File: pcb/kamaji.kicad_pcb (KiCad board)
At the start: 2 copper layers, 130 x 110 mm, 31 parts, among them J1 RJ10, J2 RJ10, J3 RJ10, J4 RJ10, J5 RJ10, Q1 TIP120, Q2 TIP120, SW1 CTRL1, SW2 CTRL2, SW3 CTRL3, U1 ATMEGA328P-PU

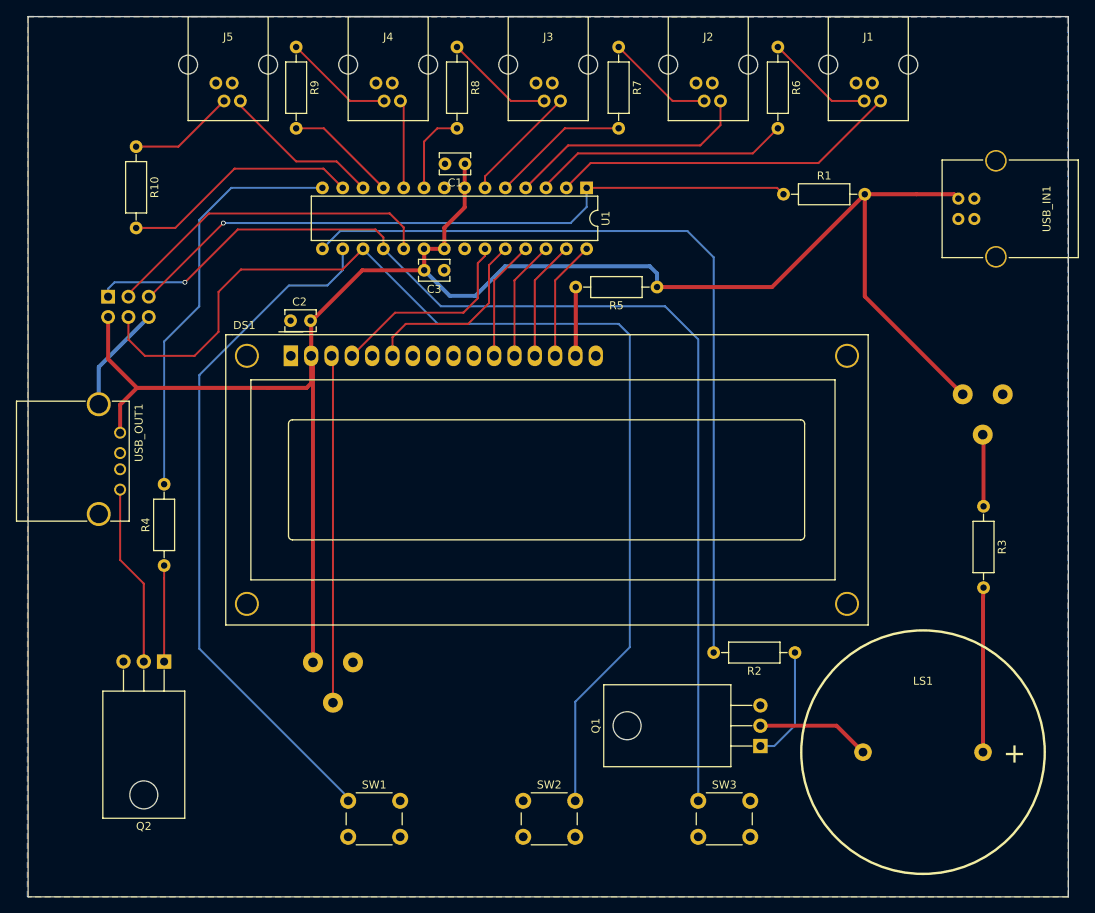
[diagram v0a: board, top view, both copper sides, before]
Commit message: add mounting holes
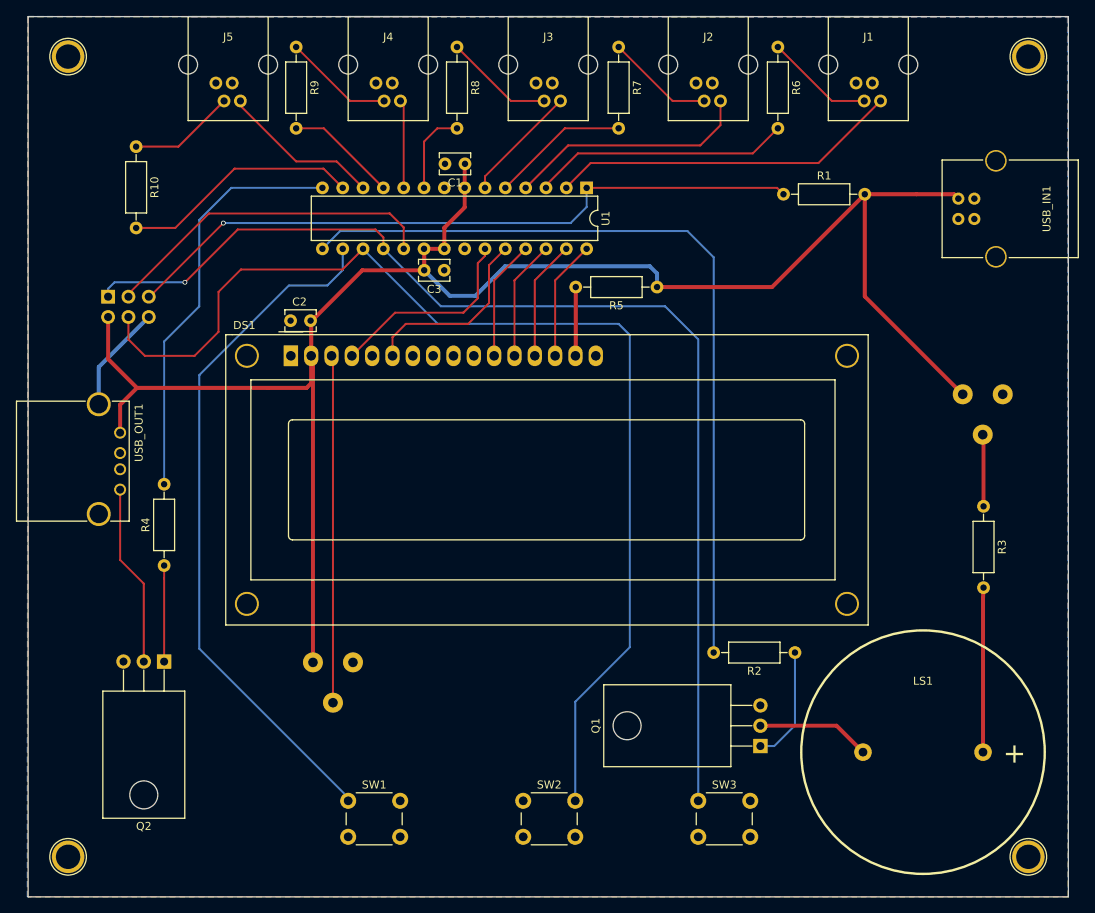
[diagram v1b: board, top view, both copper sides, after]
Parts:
- added REF**: 1pin, Connectors:1pin, F.Cu at (105.0, 35.0)
- added REF**: 1pin, Connectors:1pin, F.Cu at (225.0, 35.0)
- added REF**: 1pin, Connectors:1pin, F.Cu at (105.0, 135.0)
- added REF**: 1pin, Connectors:1pin, F.Cu at (225.0, 135.0)
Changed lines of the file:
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@@
     (links 87)
     (no_connects 3)
-    (area 99.924999 29.924999 230.075001 140.075001)
+    (area 98.074999 29.55 231.725001 140.075001)
     (thickness 1.6)
     (drawings 5)
     (tracks 185)
     (zones 0)
-    (modules 31)
+    (modules 35)
     (nets 48)
   )
@@
     (mod_text_size 1 1)
     (mod_text_width 0.15)
-    (pad_size 2 2)
-    (pad_drill 1.1)
+    (pad_size 4.064 4.064)
+    (pad_drill 3.048)
     (pad_to_mask_clearance 0.2)
-    (aux_axis_origin 106.4 35.8)
+    (aux_axis_origin 100 30)
     (visible_elements FFFFEF7F)
     (pcbplotparams
@@
     )
   )
+  (module Connectors:1pin (layer F.Cu)
+    (at 105 35)
+    (descr "module 1 pin (ou trou mecanique de percage)")
+    (tags DEV)
+    (fp_text reference REF** (at 0 -3.048) (layer F.SilkS) hide
+      (effects (font (size 1 1) (thickness 0.15)))
+    )
+    (fp_text value 1pin (at 0 3) (layer F.Fab) hide
+      (effects (font (size 1 1) (thickness 0.15)))
+    )
+    (fp_circle (center 0 0) (end 2 0.8) (layer F.Fab) (width 0.1))
+    (fp_circle (center 0 0) (end 2.6 0) (layer F.CrtYd) (width 0.05))
+    (fp_circle (center 0 0) (end 0 -2.286) (layer F.SilkS) (width 0.12))
+    (pad 1 thru_hole circle (at 0 0) (size 4.064 4.064) (drill 3.048) (layers *.Cu *.Mask))
+  )
+  (module Connectors:1pin (layer F.Cu)
+    (at 225 35)
+    (descr "module 1 pin (ou trou mecanique de percage)")
+    (tags DEV)
+    (fp_text reference REF** (at 0 -3.048) (layer F.SilkS) hide
+      (effects (font (size 1 1) (thickness 0.15)))
+    )
+    (fp_text value 1pin (at 0 3) (layer F.Fab) hide
+      (effects (font (size 1 1) (thickness 0.15)))
+    )
+    (fp_circle (center 0 0) (end 2 0.8) (layer F.Fab) (width 0.1))
+    (fp_circle (center 0 0) (end 2.6 0) (layer F.CrtYd) (width 0.05))
+    (fp_circle (center 0 0) (end 0 -2.286) (layer F.SilkS) (width 0.12))
+    (pad 1 thru_hole circle (at 0 0) (size 4.064 4.064) (drill 3.048) (layers *.Cu *.Mask))
+  )
+  (module Connectors:1pin (layer F.Cu)
+    (at 105 135)
+    (descr "module 1 pin (ou trou mecanique de percage)")
+    (tags DEV)
+    (fp_text reference REF** (at 0 -3.048) (layer F.SilkS) hide
+      (effects (font (size 1 1) (thickness 0.15)))
+    )
+    (fp_text value 1pin (at 0 3) (layer F.Fab) hide
+      (effects (font (size 1 1) (thickness 0.15)))
+    )
+    (fp_circle (center 0 0) (end 2 0.8) (layer F.Fab) (width 0.1))
+    (fp_circle (center 0 0) (end 2.6 0) (layer F.CrtYd) (width 0.05))
+    (fp_circle (center 0 0) (end 0 -2.286) (layer F.SilkS) (width 0.12))
+    (pad 1 thru_hole circle (at 0 0) (size 4.064 4.064) (drill 3.048) (layers *.Cu *.Mask))
+  )
+  (module Connectors:1pin (layer F.Cu)
+    (at 225 135)
+    (descr "module 1 pin (ou trou mecanique de percage)")
+    (tags DEV)
+    (fp_text reference REF** (at 0 -3.048) (layer F.SilkS) hide
+      (effects (font (size 1 1) (thickness 0.15)))
+    )
+    (fp_text value 1pin (at 0 3) (layer F.Fab) hide
+      (effects (font (size 1 1) (thickness 0.15)))
+    )
+    (fp_circle (center 0 0) (end 2 0.8) (layer F.Fab) (width 0.1))
+    (fp_circle (center 0 0) (end 2.6 0) (layer F.CrtYd) (width 0.05))
+    (fp_circle (center 0 0) (end 0 -2.286) (layer F.SilkS) (width 0.12))
+    (pad 1 thru_hole circle (at 0 0) (size 4.064 4.064) (drill 3.048) (layers *.Cu *.Mask))
+  )
   (gr_line (start 230 30) (end 230 140) (angle 90) (layer Edge.Cuts) (width 0.15))

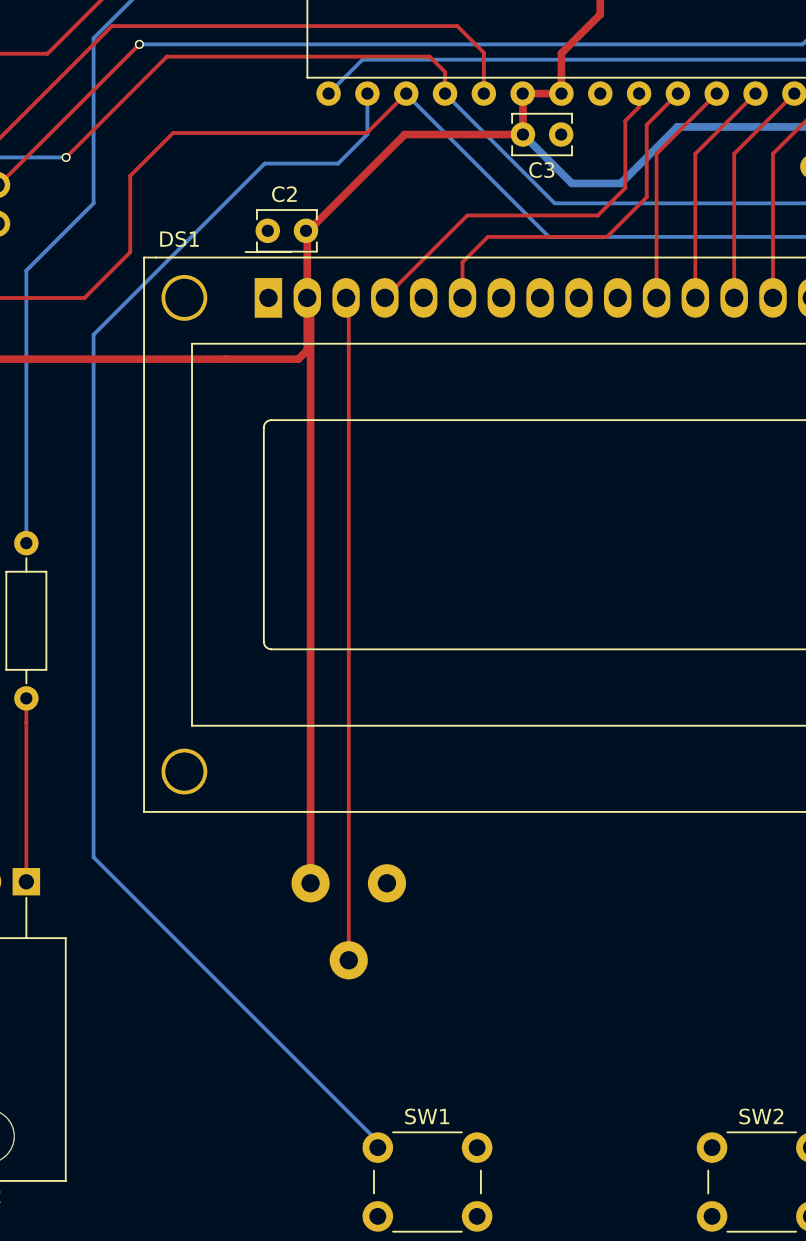
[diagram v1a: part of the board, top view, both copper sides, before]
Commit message: move a few tracks
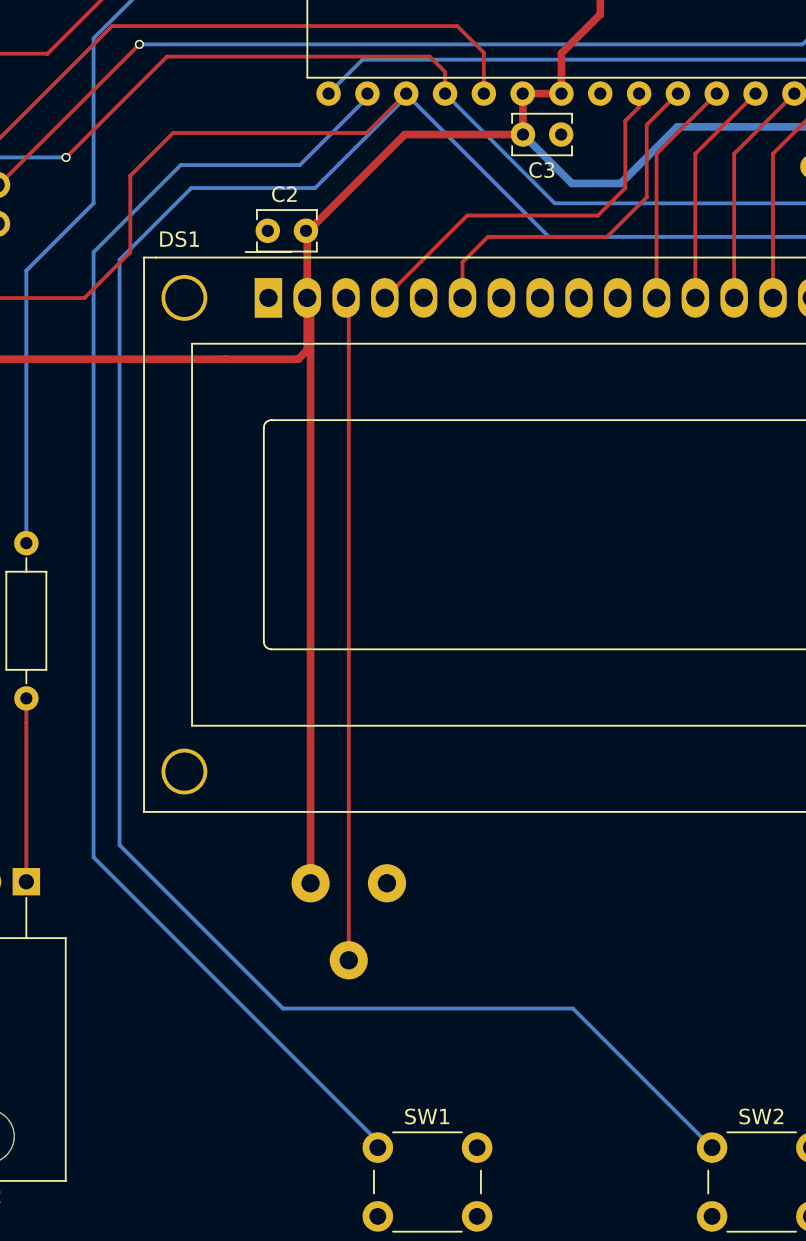
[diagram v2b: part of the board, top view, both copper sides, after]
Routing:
- net CBTN2: track 140.3 -> 249.0 mm
- net CBTN1: track 86.9 -> 89.1 mm
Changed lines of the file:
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@@
   (general
     (links 87)
-    (no_connects 3)
+    (no_connects 2)
     (area 98.074999 29.55 231.725001 140.075001)
     (thickness 1.6)
     (drawings 5)
-    (tracks 185)
+    (tracks 194)
     (zones 0)
     (modules 35)
@@
   (segment (start 145.2 54.6) (end 146.94 56.34) (width 0.25) (layer F.Cu) (net 23))
   (segment (start 146.94 56.34) (end 146.94 59.02) (width 0.25) (layer F.Cu) (net 23))
+  (segment (start 141.86 59.02) (end 141.86 59.24) (width 0.25) (layer B.Cu) (net 24) (status C00000))
+  (segment (start 141.86 59.24) (end 135.9 65.2) (width 0.25) (layer B.Cu) (net 24) (status 400000))
+  (segment (start 152.775 118.9) (end 161.875 128) (width 0.25) (layer B.Cu) (net 24) (status 800000))
+  (segment (start 133.8 118.9) (end 152.775 118.9) (width 0.25) (layer B.Cu) (net 24))
+  (segment (start 123.1 108.2) (end 133.8 118.9) (width 0.25) (layer B.Cu) (net 24))
+  (segment (start 123.1 69.9) (end 123.1 108.2) (width 0.25) (layer B.Cu) (net 24))
+  (segment (start 127.8 65.2) (end 123.1 69.9) (width 0.25) (layer B.Cu) (net 24))
+  (segment (start 135.9 65.2) (end 127.8 65.2) (width 0.25) (layer B.Cu) (net 24))
   (segment (start 141.86 59.02) (end 141.86 59.06) (width 0.25) (layer B.Cu) (net 24))
   (segment (start 141.86 59.06) (end 151.2 68.4) (width 0.25) (layer B.Cu) (net 24))
@@
   (segment (start 173.8 43.96) (end 167.08 43.96) (width 0.25) (layer F.Cu) (net 35))
   (segment (start 167.08 43.96) (end 159.64 51.4) (width 0.25) (layer F.Cu) (net 35))
+  (segment (start 139.32 59.02) (end 139.32 59.28) (width 0.25) (layer B.Cu) (net 37) (status C00000))
+  (segment (start 139.32 59.28) (end 134.9 63.7) (width 0.25) (layer B.Cu) (net 37) (status 400000))
+  (segment (start 134.9 63.7) (end 127.1 63.7) (width 0.25) (layer B.Cu) (net 37))
+  (segment (start 127.1 63.7) (end 121.4 69.4) (width 0.25) (layer B.Cu) (net 37))
+  (segment (start 121.4 69.4) (end 121.4 109) (width 0.25) (layer B.Cu) (net 37))
+  (segment (start 121.4 109) (end 140 127.6) (width 0.25) (layer B.Cu) (net 37) (status 800000))
+  (segment (start 140 127.6) (end 140 128) (width 0.25) (layer B.Cu) (net 37) (status C00000))
   (segment (start 140 128) (end 140 127.6) (width 0.25) (layer B.Cu) (net 37))
-  (segment (start 140 127.6) (end 121.4 109) (width 0.25) (layer B.Cu) (net 37))
-  (segment (start 121.4 109) (end 121.4 74.8) (width 0.25) (layer B.Cu) (net 37))
-  (segment (start 121.4 74.8) (end 132.6 63.6) (width 0.25) (layer B.Cu) (net 37))
-  (segment (start 132.6 63.6) (end 137.4 63.6) (width 0.25) (layer B.Cu) (net 37))
-  (segment (start 137.4 63.6) (end 139.32 61.68) (width 0.25) (layer B.Cu) (net 37))
-  (segment (start 139.32 61.68) (end 139.32 59.02) (width 0.25) (layer B.Cu) (net 37))
   (segment (start 157.1 51.4) (end 157.1 49.97) (width 0.25) (layer F.Cu) (net 38))
   (segment (start 157.1 49.97) (end 166.53 40.54) (width 0.25) (layer F.Cu) (net 38))

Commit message: move another resistor
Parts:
- moved R10 7.73 mm to (115.9, 38.9)
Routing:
- net PLED5: track 29.9 -> 24.4 mm
- net Net-(J5-Pad2): track 13.6 -> 9.35 mm
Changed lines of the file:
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@@
     (area 98.074999 29.55 231.725001 140.075001)
     (thickness 1.6)
-    (drawings 5)
-    (tracks 194)
+    (drawings 4)
+    (tracks 192)
     (zones 0)
     (modules 35)
@@
   )
   (module Resistors_THT:R_Axial_DIN0207_L6.3mm_D2.5mm_P10.16mm_Horizontal (layer F.Cu)
-    (at 113.5 46.25 270)
+    (at 115.9 38.9 270)
     (descr "Resistor, Axial_DIN0207 series, Axial, Horizontal, pin pitch=10.16mm, 0.25W = 1/4W, length*diameter=6.3*2.5mm^2, http://cdn-reichelt.de/documents/datenblatt/B400/1_4W%23YAG.pdf")
     (tags "Resistor Axial_DIN0207 series Axial Horizontal pin pitch 10.16mm 0.25W = 1/4W length 6.3mm diameter 2.5mm")
@@
   (gr_line (start 100 30) (end 230 30) (angle 90) (layer Edge.Cuts) (width 0.15))
   (gr_line (start 100 140) (end 100 30) (angle 90) (layer Edge.Cuts) (width 0.15))
-  (target plus (at 165 95.08) (size 5) (width 0.15) (layer Edge.Cuts))
   (gr_line (start 230 140) (end 100 140) (angle 90) (layer Edge.Cuts) (width 0.15))
   (segment (start 178.6 63.8) (end 178.6 62.1) (width 0.5) (layer B.Cu) (net 1))
@@
   (segment (start 144.49 40.54) (end 140.24 40.54) (width 0.25) (layer F.Cu) (net 20))
   (segment (start 140.24 40.54) (end 133.5 33.8) (width 0.25) (layer F.Cu) (net 20))
-  (segment (start 113.5 46.25) (end 118.78 46.25) (width 0.25) (layer F.Cu) (net 21))
-  (segment (start 118.78 46.25) (end 124.49 40.54) (width 0.25) (layer F.Cu) (net 21))
-  (segment (start 113.5 46.25) (end 113.78 46.25) (width 0.25) (layer F.Cu) (net 21))
+  (segment (start 124.49 40.54) (end 117.54 40.54) (width 0.25) (layer F.Cu) (net 21) (status 400000))
+  (segment (start 117.54 40.54) (end 115.9 38.9) (width 0.25) (layer F.Cu) (net 21) (status 800000))
+  (segment (start 124.43 40.6) (end 124.49 40.54) (width 0.25) (layer F.Cu) (net 21))
   (segment (start 144.4 59.02) (end 144.4 57.6) (width 0.25) (layer F.Cu) (net 22))
   (segment (start 144.4 57.6) (end 143.4 56.6) (width 0.25) (layer F.Cu) (net 22))
@@
   (segment (start 145.2 54.6) (end 146.94 56.34) (width 0.25) (layer F.Cu) (net 23))
   (segment (start 146.94 56.34) (end 146.94 59.02) (width 0.25) (layer F.Cu) (net 23))
-  (segment (start 141.86 59.02) (end 141.86 59.24) (width 0.25) (layer B.Cu) (net 24) (status C00000))
-  (segment (start 141.86 59.24) (end 135.9 65.2) (width 0.25) (layer B.Cu) (net 24) (status 400000))
-  (segment (start 152.775 118.9) (end 161.875 128) (width 0.25) (layer B.Cu) (net 24) (status 800000))
+  (segment (start 141.86 59.02) (end 141.86 59.24) (width 0.25) (layer B.Cu) (net 24))
+  (segment (start 141.86 59.24) (end 135.9 65.2) (width 0.25) (layer B.Cu) (net 24))
+  (segment (start 152.775 118.9) (end 161.875 128) (width 0.25) (layer B.Cu) (net 24))
   (segment (start 133.8 118.9) (end 152.775 118.9) (width 0.25) (layer B.Cu) (net 24))
   (segment (start 123.1 108.2) (end 133.8 118.9) (width 0.25) (layer B.Cu) (net 24))
@@
   (segment (start 173.8 43.96) (end 167.08 43.96) (width 0.25) (layer F.Cu) (net 35))
   (segment (start 167.08 43.96) (end 159.64 51.4) (width 0.25) (layer F.Cu) (net 35))
-  (segment (start 139.32 59.02) (end 139.32 59.28) (width 0.25) (layer B.Cu) (net 37) (status C00000))
-  (segment (start 139.32 59.28) (end 134.9 63.7) (width 0.25) (layer B.Cu) (net 37) (status 400000))
+  (segment (start 139.32 59.02) (end 139.32 59.28) (width 0.25) (layer B.Cu) (net 37))
+  (segment (start 139.32 59.28) (end 134.9 63.7) (width 0.25) (layer B.Cu) (net 37))
   (segment (start 134.9 63.7) (end 127.1 63.7) (width 0.25) (layer B.Cu) (net 37))
   (segment (start 127.1 63.7) (end 121.4 69.4) (width 0.25) (layer B.Cu) (net 37))
   (segment (start 121.4 69.4) (end 121.4 109) (width 0.25) (layer B.Cu) (net 37))
-  (segment (start 121.4 109) (end 140 127.6) (width 0.25) (layer B.Cu) (net 37) (status 800000))
-  (segment (start 140 127.6) (end 140 128) (width 0.25) (layer B.Cu) (net 37) (status C00000))
+  (segment (start 121.4 109) (end 140 127.6) (width 0.25) (layer B.Cu) (net 37))
+  (segment (start 140 127.6) (end 140 128) (width 0.25) (layer B.Cu) (net 37))
   (segment (start 140 128) (end 140 127.6) (width 0.25) (layer B.Cu) (net 37))
   (segment (start 157.1 51.4) (end 157.1 49.97) (width 0.25) (layer F.Cu) (net 38))
@@
   (segment (start 133.5 48.1) (end 138.56 48.1) (width 0.25) (layer F.Cu) (net 42))
   (segment (start 138.56 48.1) (end 141.86 51.4) (width 0.25) (layer F.Cu) (net 42))
-  (segment (start 113.5 56.41) (end 118.39 56.41) (width 0.25) (layer F.Cu) (net 43))
-  (segment (start 136.92 49) (end 139.32 51.4) (width 0.25) (layer F.Cu) (net 43))
-  (segment (start 125.8 49) (end 136.92 49) (width 0.25) (layer F.Cu) (net 43))
-  (segment (start 118.39 56.41) (end 125.8 49) (width 0.25) (layer F.Cu) (net 43))
+  (segment (start 115.9 49.06) (end 136.98 49.06) (width 0.25) (layer F.Cu) (net 43) (status 400000))
+  (segment (start 136.98 49.06) (end 139.32 51.4) (width 0.25) (layer F.Cu) (net 43) (status 800000))
   (zone (net 2) (net_name GND) (layer F.Cu) (hatch edge 0.508)
     (connect_pads (clearance 0.508))
